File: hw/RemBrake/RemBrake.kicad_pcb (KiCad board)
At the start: 2 copper layers, 40 x 80 mm, 133 parts, among them J1 Screw_Terminal_01x02, J2 Conn_01x03_MountingPin, J3 Screw_Terminal_01x04, J4 Conn_01x08_MountingPin, J5 Conn_01x04_MountingPin, J6 Conn_01x03_MountingPin, J7 Conn_01x03, J8 Conn_01x07, J9 Conn_01x07, Q1 SiS415DNT, Q10 BC337, Q11 BC847, Q12 BC847, Q13 SiS415DNT, Q14 BC337, Q2 BC337, Q3 BC847, Q4 BC337, Q5 BC847, Q6 BC337, Q7 BC847, Q8 BC337, Q9 BC847, U1 TPS62140, U2 BD5230G-TR, U3 XC6220B331MR, U4 MAX40200AUK, U5 LM555xN, U6 BD5230G-TR, U7 LTC2943IDD#TRPBF, U8 MAX40200AUK

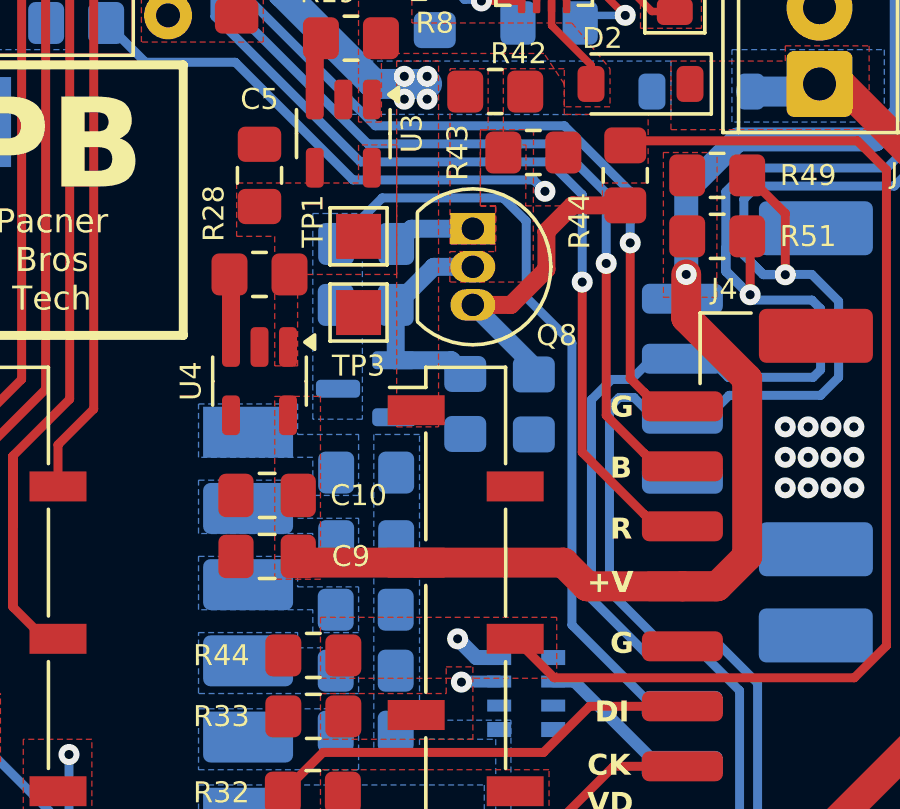
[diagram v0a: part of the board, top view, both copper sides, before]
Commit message: updated schematics and pcb - smd transistor was not connected to resistor to limit current through buzzer
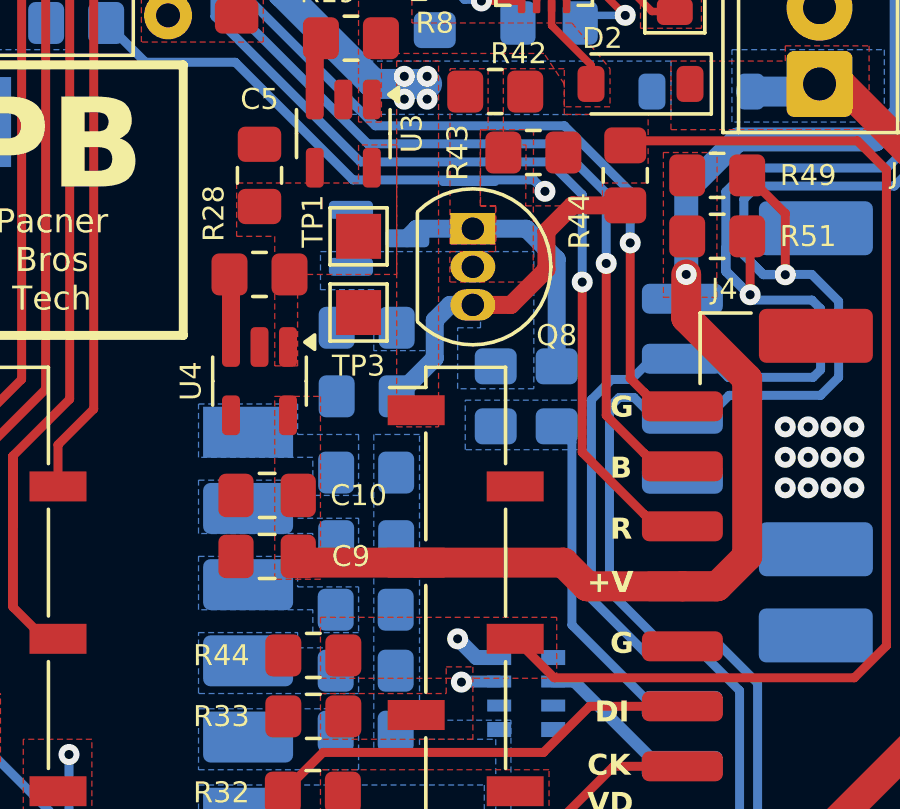
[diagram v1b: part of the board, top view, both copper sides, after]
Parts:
- C12: value 680pF -> 0.1uF
- R31, R32: value 220 -> 0R
- R62: value 0R -> 10k
- moved R46 8.13 mm to (144.6, 118.9), turned to 90 degrees
- moved R48 5.58 mm to (138.3, 118.9), turned to 0 degrees
- moved R45 5.30 mm to (142.6, 118.9), turned to 90 degrees
- moved Q9 5.03 mm to (138.7, 113.7), turned to 0 degrees
- moved R47 4.15 mm to (138.3, 116.6), turned to 0 degrees
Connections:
- Q9 pad 3: /control_connector/BUZZER -> Net-(Q8-C)
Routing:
- net /control_connector/BUZZER: track 26.2 -> 11.9 mm
- net Net-(Q8-B): track 7.52 -> 0.00 mm
- net Net-(Q8-C): track 2.77 -> 9.11 mm
- net Net-(Q8-E): track 10.4 -> 11.7 mm
- added copper zone on B.Cu, net Net-(Q8-B)

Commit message: removed hopefully last redundant components and updated versions of pcb and schematics
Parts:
- removed the R44 at (136.5, 127.6)
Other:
- board text added: "RemBrake rev. 3.1 (DMY-200725)"
- board text removed: "RemBrake rev. 3.0 (DMY-010725)"

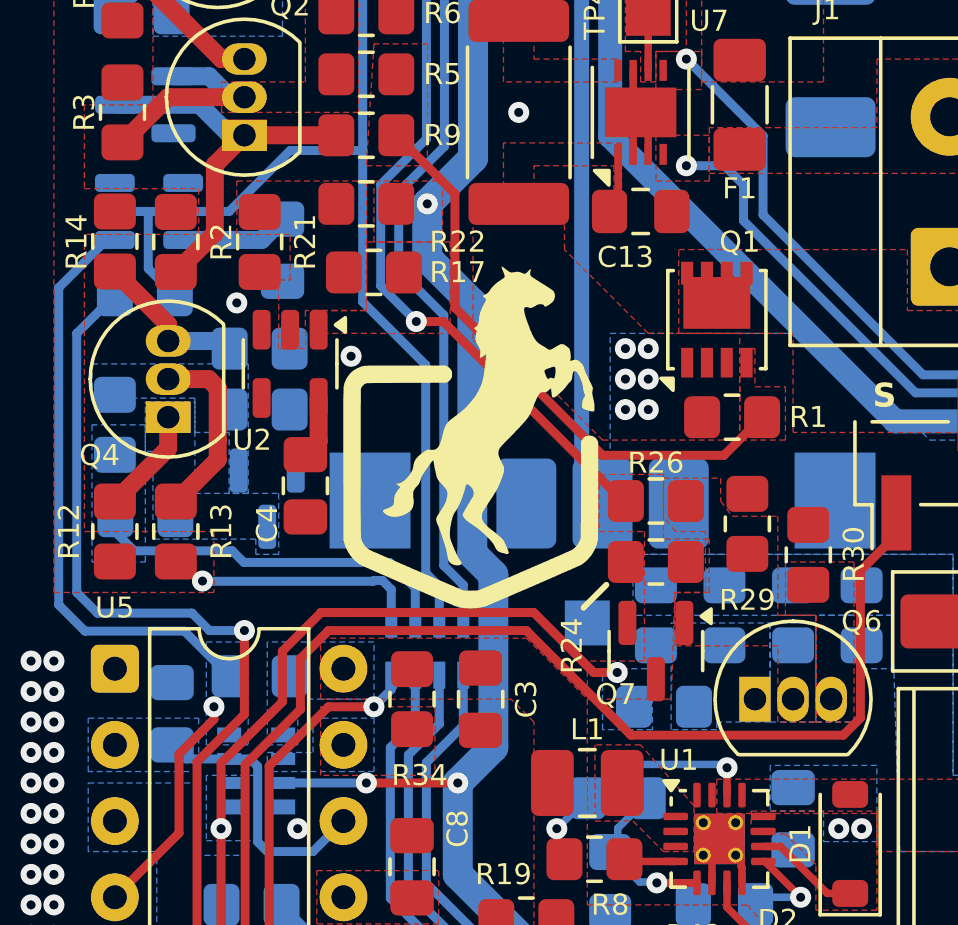
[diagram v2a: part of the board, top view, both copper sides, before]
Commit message: fixed mismatches found by parity check (drc)
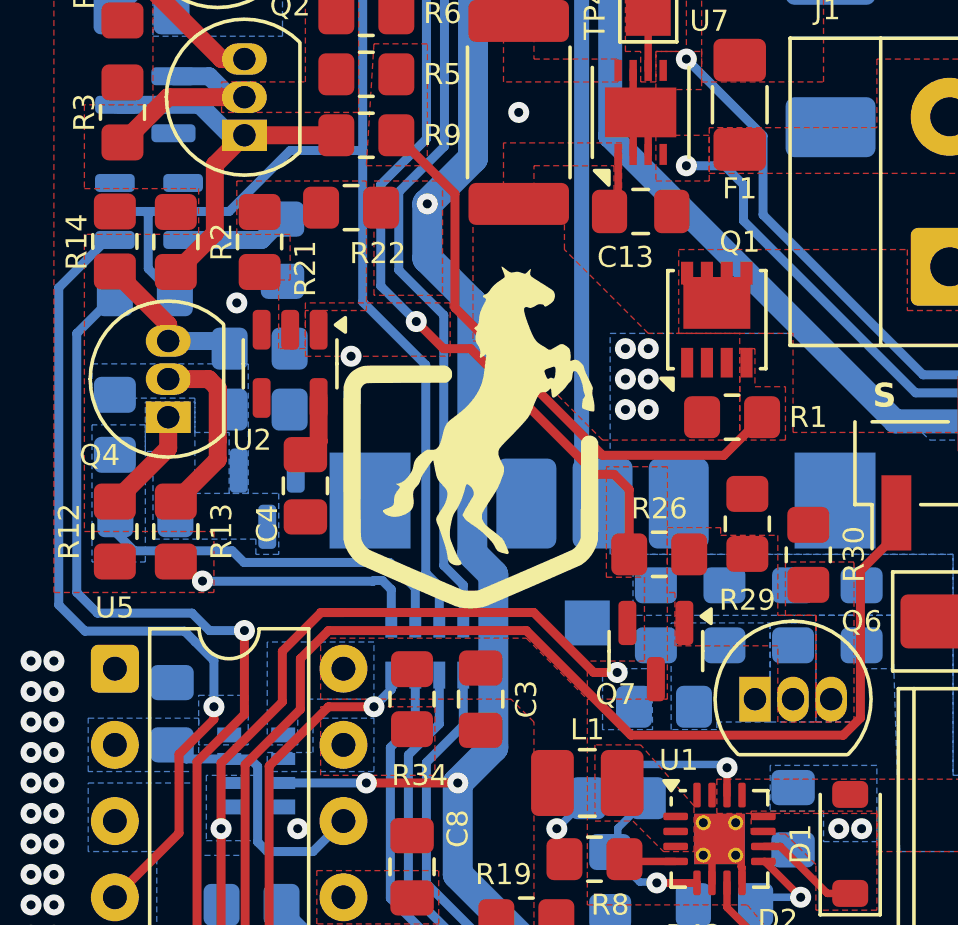
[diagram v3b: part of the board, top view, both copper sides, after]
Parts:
- removed the R17 at (132.7, 85.4)
- removed the R24 at (142.1, 95.0)
- removed the R39 at (128.9, 98.9)
- moved R26 1.78 mm to (142.2, 94.8)
- moved R22 0.52 mm to (131.9, 83.2)
- renumbered REF** to LOGO1, REF** to LOGO2
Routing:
- net /brake_control/ENABLE: track 74.0 -> 76.1 mm
- net /brake_control/BEEP: track 27.5 -> 28.3 mm

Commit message: 5k resistors replaced by 5k1 resistors
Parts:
- R24, R3: value 5k -> 5k1
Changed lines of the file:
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@@
 			)
 		)
-		(property "Value" "5k"
+		(property "Value" "5k1"
 			(at 0 1.65 90)
 			(layer "F.Fab")
@@
 			)
 		)
-		(property "Value" "5k"
+		(property "Value" "5k1"
 			(at 0 -1.65 90)
 			(layer "B.Fab")

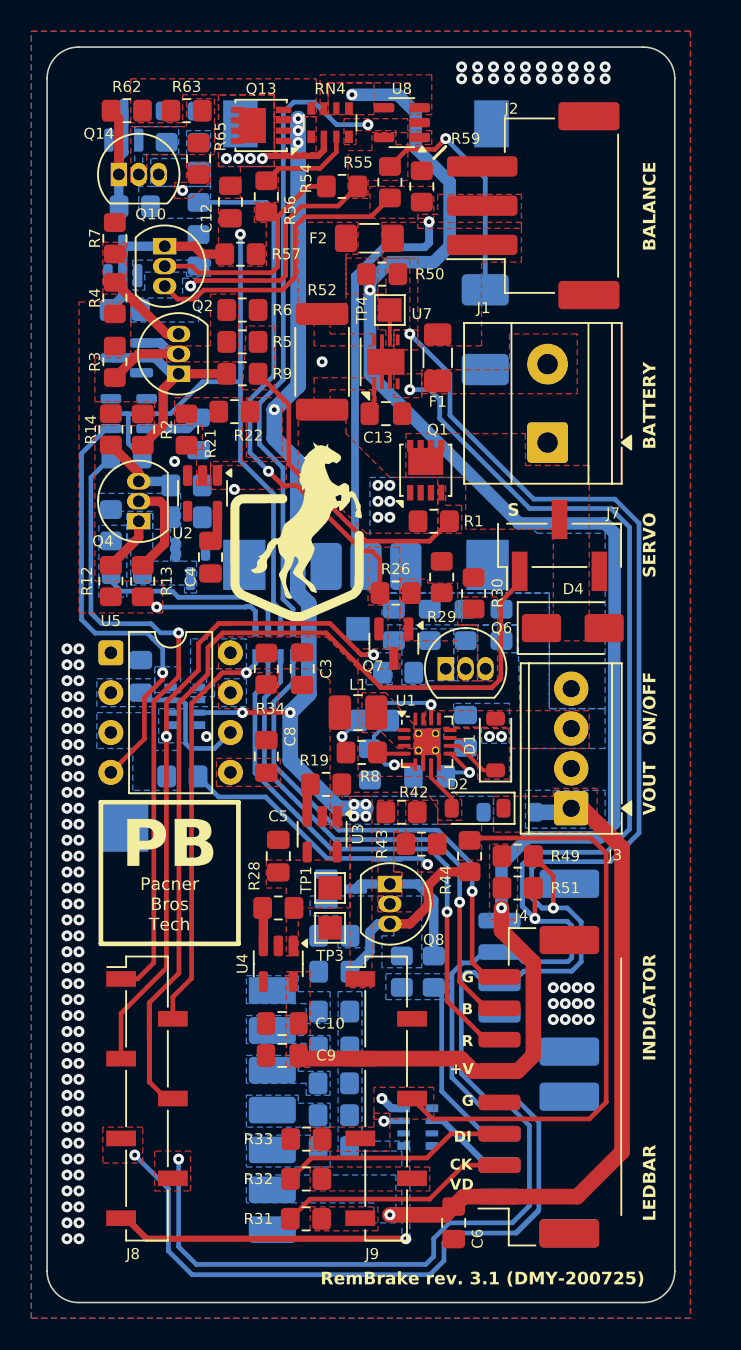
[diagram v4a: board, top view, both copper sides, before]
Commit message: updated pcb and added Notes about possible faults
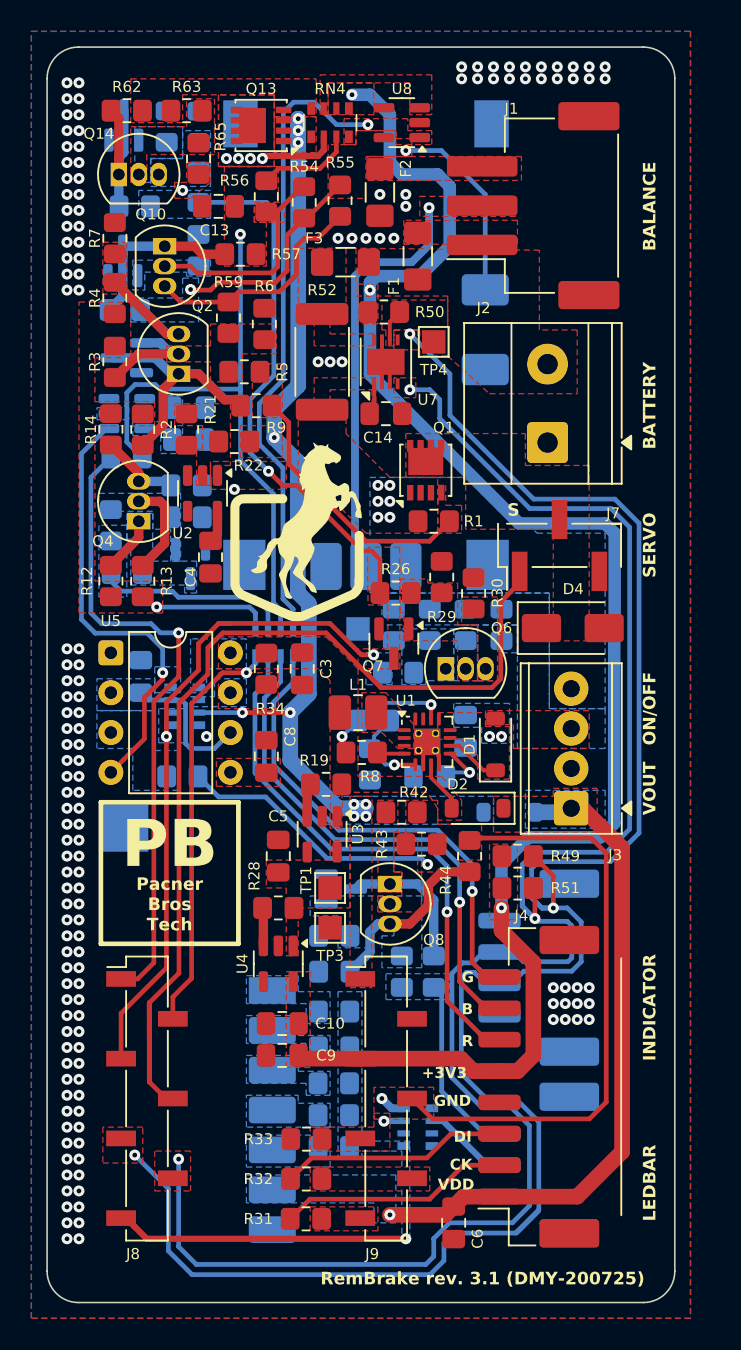
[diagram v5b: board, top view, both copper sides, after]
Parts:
- added C11: 0.1uF, Capacitor_SMD:C_0805_2012Metric_Pad1.18x1.45mm_HandSolder, B.Cu at (129.0, 85.0)
- added F3: 10A / 24V, Fuse:Fuse_1206_3216Metric_Pad1.42x1.75mm_HandSolder, F.Cu at (139.0, 73.7)
- C10, C9: value 22uF -> 0.1uF
- R10: value 536k -> 560k
- moved R59 14.9 mm to (131.6, 77.2), turned to 90 degrees
- moved F1 6.60 mm to (143.6, 73.3), turned to 90 degrees
- moved TP4 3.45 mm to (144.6, 78.8)
- moved R55 3.39 mm to (138.7, 69.8)
- moved F2 3.00 mm to (141.2, 69.3), turned to 90 degrees
- moved R54 2.62 mm to (136.4, 69.9), turned to 90 degrees
- moved R50 2.42 mm to (141.5, 76.9)
- moved R9 2.22 mm to (133.3, 82.8)
- moved R5 1.91 mm to (132.6, 80.7)
- moved R22 1.91 mm to (131.9, 85.1)
- moved C12 1.79 mm to (129.0, 83.0), turned to 0 degrees
- moved R6 1.66 mm to (133.8, 77.6), turned to -90 degrees
- moved C13 0.81 mm to (130.9, 70.2), turned to 180 degrees
- moved U6 0.12 mm to (125.1, 83.4)
- renumbered C11 to C12, C12 to C13, C13 to C14, J2 to J1, J1 to J2
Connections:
- F1 pad 1: Net-(J2-Pin_1) -> Net-(J2-Pin_2)
- F1 pad 2: Net-(J1-Pin_2) -> Net-(J1-Pin_1)
- F2 pad 1: /power_manager/BAT+ -> GND
- F2 pad 2: Net-(J2-Pin_1) -> Net-(J1-Pin_3)
- J1 pad 1: Net-(J2-Pin_1) -> Net-(J1-Pin_1)
- J1 pad 3: GND -> Net-(J1-Pin_3)
- J2 pad 2: Net-(J1-Pin_2) -> Net-(J2-Pin_2)
- U1 pad 13: /power_switch/ON/OFF -> Net-(D1-K)
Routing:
- net Net-(Q10-E): track 19.3 -> 14.9 mm
- net Net-(M2-LED): track 30.2 -> 25.9 mm
- net Net-(U6-CT): track 3.60 -> 0.00 mm
- net Net-(Q1-G): track 19.4 -> 17.0 mm
- net Net-(Q2-C): track 13.2 -> 15.0 mm
- net Net-(Q10-B): track 14.6 -> 13.1 mm
- net /power_manager/BM: track 25.7 -> 26.7 mm
- net GND: vias 112 -> 149
- added copper zone on B.Cu, net /brake_control/CHARGING
- added copper zone on F.Cu, net Net-(J1-Pin_1)
- added copper zone on F.Cu, net Net-(J1-Pin_3)
- added copper zone on F.Cu, net Net-(J2-Pin_2)
- added copper zone on F.Cu, net Net-(Q10-B)
- added copper zone on B.Cu, net Net-(U6-CT)
- removed copper zone on F.Cu, net Net-(J1-Pin_2)
- removed copper zone on F.Cu, net Net-(J2-Pin_1)
- removed copper zone on F.Cu, net Net-(Q10-E)
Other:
- board text added: "+3V3"
- board text added: "VDD"
- board text removed: "+V"
- board text removed: "VD"

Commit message: changed diode footprint at the input of the dc/dc, use the same diode as servo clamping diode
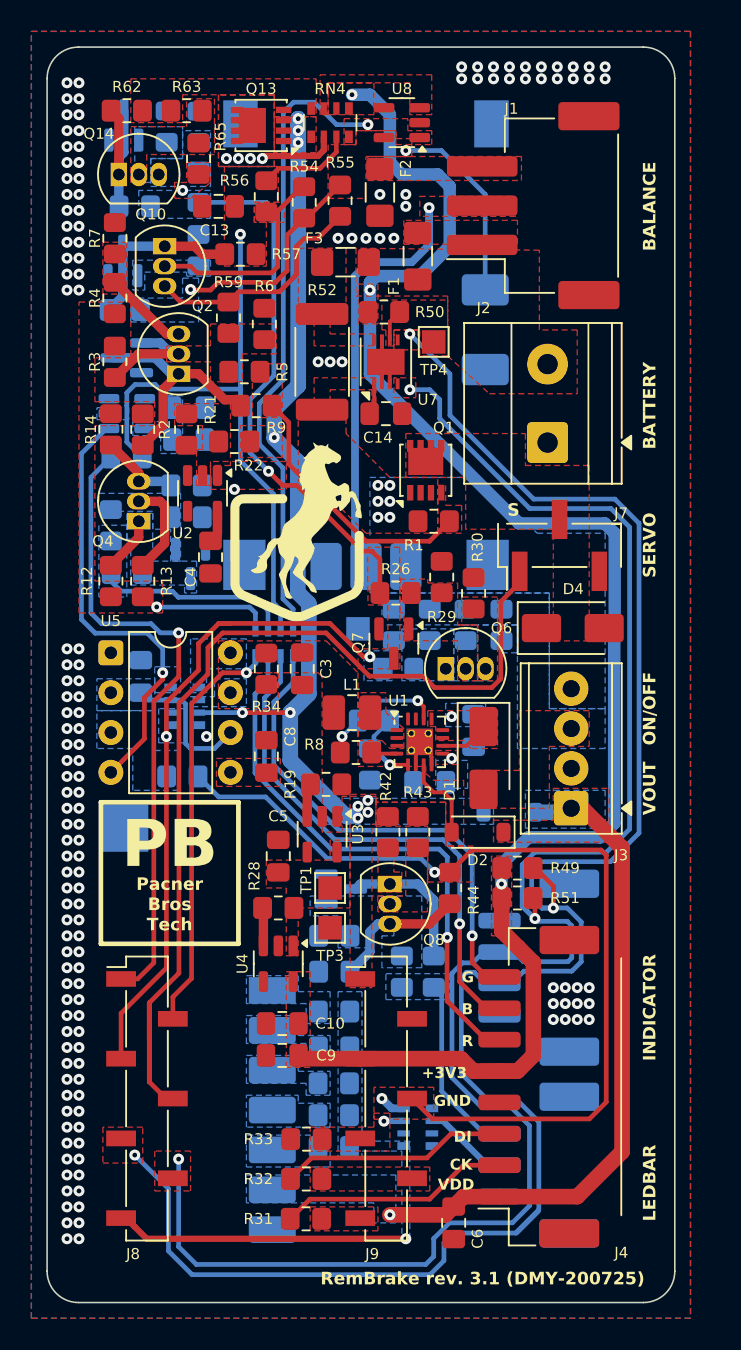
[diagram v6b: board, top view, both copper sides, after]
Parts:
- D1: footprint Diode_SMD:D_SOD-123 -> Diode_SMD:D_SMA
- R64, R65, R66: value 5k1 -> 10k
- moved R44 2.40 mm to (145.7, 113.6)
- moved R42 1.54 mm to (141.7, 110.0), turned to 90 degrees
- moved D2 1.52 mm to (147.4, 110.0)
- moved D1 1.15 mm to (147.8, 105.3), turned to -90 degrees
- moved R43 0.80 mm to (143.6, 110.0), turned to -90 degrees
- moved R49 0.76 mm to (150.0, 112.3)
- moved R51 0.64 mm to (150.0, 114.2)
- moved C1 0.51 mm to (147.2, 103.6)
- moved U1 0.47 mm to (143.7, 104.3)
- moved C2 0.38 mm to (144.4, 106.9)
- moved L1 0.38 mm to (139.4, 102.4)
- moved R8 0.37 mm to (139.7, 104.9)
- moved R27 0.25 mm to (142.4, 99.6)
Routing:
- net Net-(U1-SS/TR): track 3.35 -> 0.00 mm
- net Net-(Q8-E): track 11.7 -> 8.89 mm
- net /brake_control/BUZZ: track 57.0 -> 59.1 mm
- net +5V: track 10.8 -> 12.5 mm
- net /brake_control/I2C.SDA: track 124.7 -> 124.1 mm
- net /brake_control/I2C.SCL: track 114.8 -> 114.1 mm
- net +3V3: track 102.4 -> 103.0 mm
- net /power_switch/VBUS: track 56.2 -> 55.7 mm
- net Net-(U1-FB): track 6.73 -> 7.29 mm
- net GND: track 8.68 -> 8.17 mm
- net Net-(D1-K): track 3.42 -> 3.18 mm, vias 2 -> 1
- added copper zone on B.Cu, net Net-(U1-SS/TR)
- added copper zone on F.Cu, net Net-(U1-SS/TR)

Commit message: added protection diode at the power input
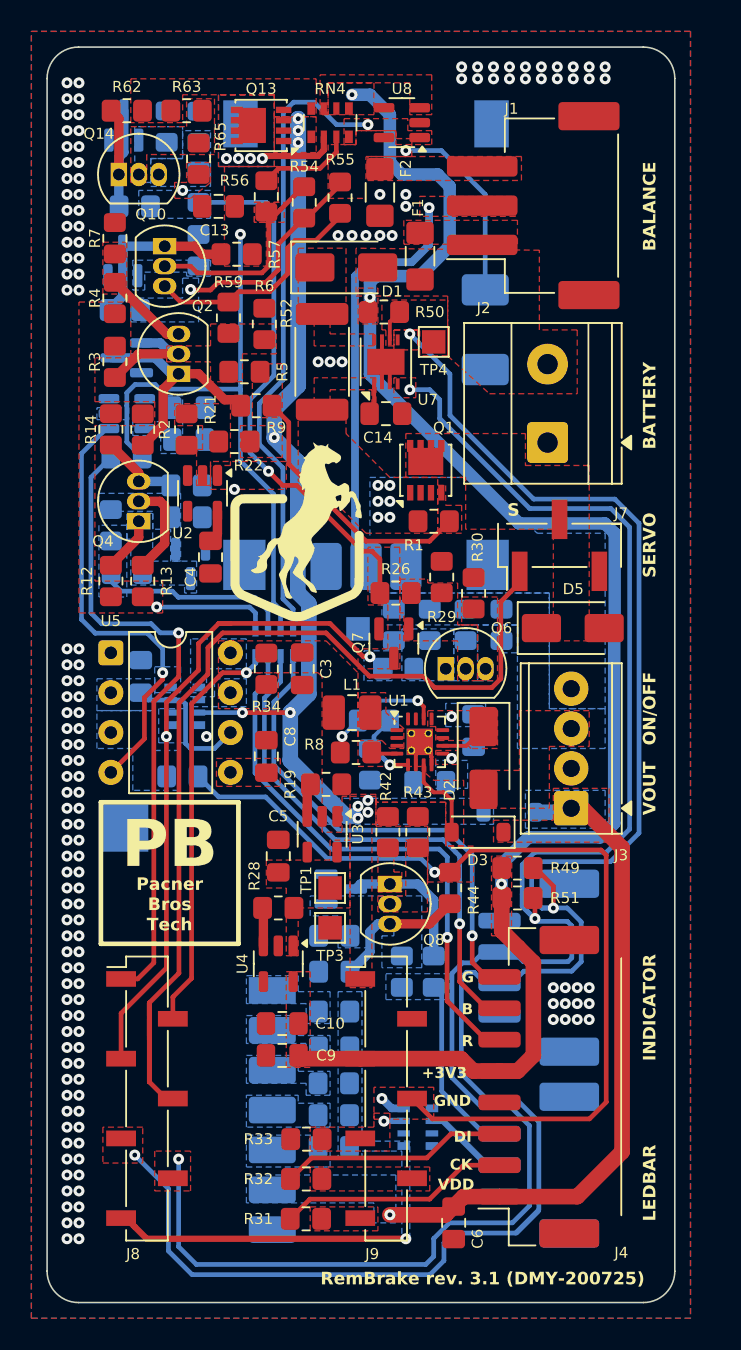
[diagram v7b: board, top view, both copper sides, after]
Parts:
- removed F3: 10A / 24V, Fuse:Fuse_1206_3216Metric_Pad1.42x1.75mm_HandSolder
- added D1: MBR0520, Diode_SMD:D_SMA, F.Cu at (139.1, 74.0)
- moved R57 0.24 mm to (132.1, 73.2)
- moved R55 0.19 mm to (138.7, 69.6)
- moved F1 0.14 mm to (143.8, 73.3)
- renumbered D1 to D2, D2 to D3, D3 to D4, D4 to D5
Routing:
- net Net-(Q10-B): track 13.1 -> 13.8 mm
